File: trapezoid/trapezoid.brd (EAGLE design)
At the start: 59.7 x 28.6 mm, 32 parts, among them IC2 LGD20H, U1 MMA8452Q, U2 microSD, U4 MCP73831, Y1 CRYSTAL.ABS25

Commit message: small tweak
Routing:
- net GND: vias 9 -> 10
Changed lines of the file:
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@@
 <via x="14.605" y="19.685" extent="1-16" drill="0.508"/>
 <via x="20.32" y="5.08" extent="1-16" drill="0.508"/>
+<via x="57.15" y="16.51" extent="1-16" drill="0.508"/>
 </signal>
 <signal name="SCL">

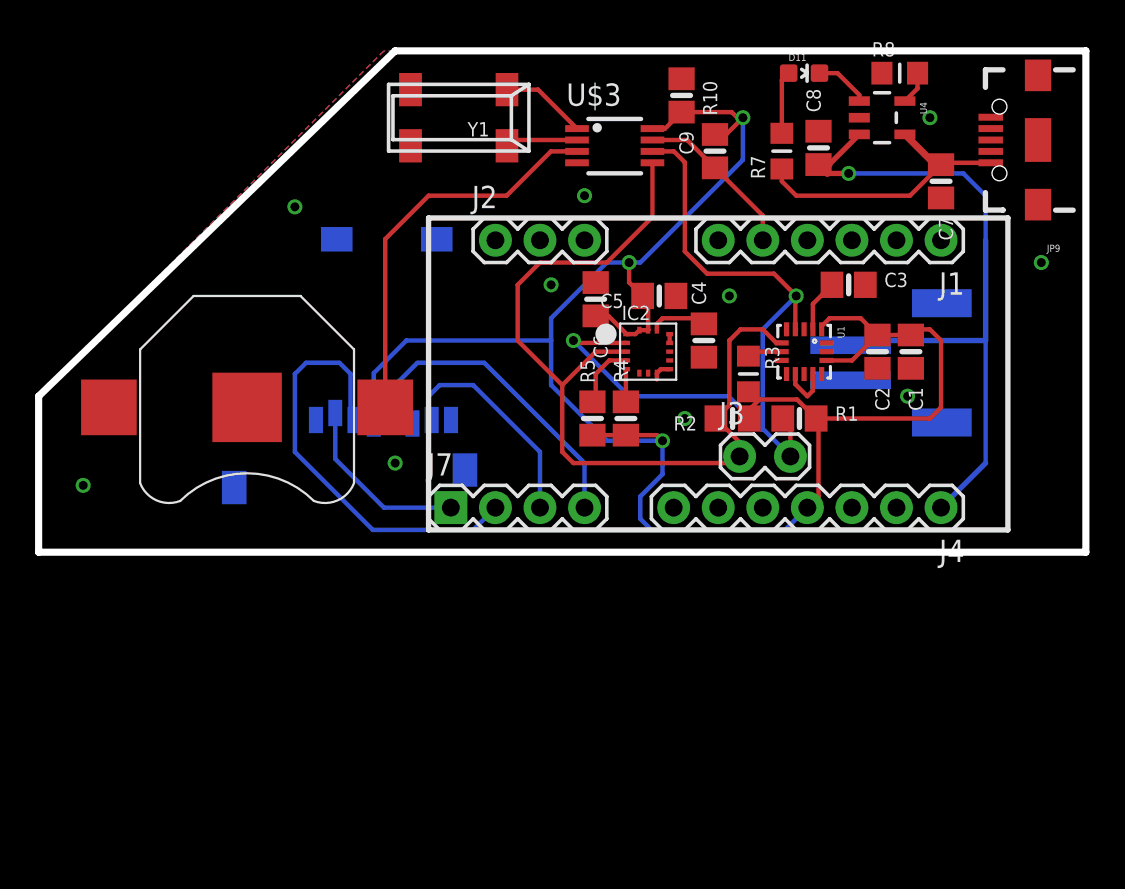
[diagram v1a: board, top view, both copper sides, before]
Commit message: changed gyro in schematic
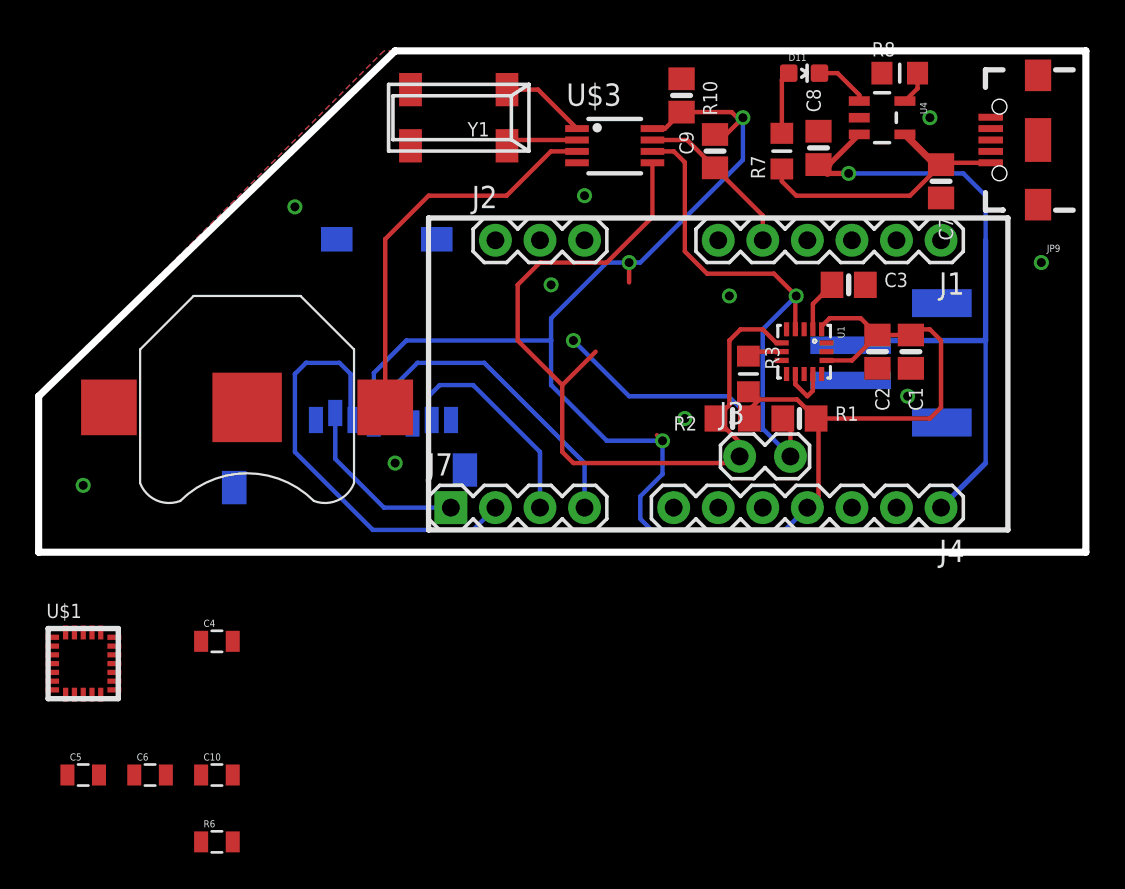
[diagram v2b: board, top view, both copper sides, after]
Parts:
- removed IC2: LGD20H, microbuilder:L3GD20H_LGA16L
- removed R4, R5: 10K, microbuilder:0805-NO
- added C10: 1.0uF, SparkFun-Passives:0805
- added R6: 47k, SparkFun-Passives:0805
- added U$1: FXAS21002, sharkdunio:24QFN
- C4, C6: device microbuilder:0805-NO -> SparkFun-Passives:0805
- C5: value 10uF -> 0.1uF; device microbuilder:0805-NO -> SparkFun-Passives:0805
- moved C5 42.7 mm to (2.54, -12.7), turned to 0 degrees
- moved C6 37.2 mm to (6.35, -12.7), turned to 0 degrees
- moved C4 32.6 mm to (10.2, -5.08), turned to 0 degrees
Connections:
- removed net CS_3.3V: IC2.5, R4.2
- removed net SDO/SAO: IC2.4, R5.2
- new net INT2: U$1.2
- new net N$9: R6.1, U$1.4
- net +3V3: now also C10.1, C4.2, C6.1, R6.2, U$1.15, U$1.17, U$1.18; no longer C5.2, C6.2, IC2.1, IC2.15, IC2.16, R4.1, R5.1
- net GND: now also C10.2, C5.2, C6.2, U$1.1, U$1.10, U$1.13, U$1.14, U$1.19, U$1.20, U$1.21, U$1.22, U$1.23, U$1.24, U$1.5, U$1.6, U$1.7, U$1.8, U$1.9; no longer C5.1, C6.1, IC2.10, IC2.11, IC2.12, IC2.13, IC2.8, IC2.9
- net N$3: now also C5.1, U$1.16; no longer C4.2, IC2.14
- net SCL: now also U$1.11; no longer IC2.2
- net SDA: now also U$1.12; no longer IC2.3
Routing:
- net +3V3: track 111.1 -> 100.7 mm
- net SDO/SAO: track 3.75 -> 0.00 mm
- net N$3: track 3.30 -> 0.00 mm
- net SCL: track 45.5 -> 42.6 mm
- net CS_3.3V: track 1.88 -> 0.00 mm
- net SDA: track 49.0 -> 47.2 mm
- net GND: track 4.90 -> 3.22 mm

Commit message: fully routed board
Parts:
- removed R6: 47k, SparkFun-Passives:0805
- added R4: 47K, microbuilder:0805-NO
- C10: value 1.0uF -> 0.1uF; device SparkFun-Passives:0805 -> microbuilder:0805-NO
- C4, C5, C6: device SparkFun-Passives:0805 -> microbuilder:0805-NO
- moved C5 38.2 mm to (31.1, 12.7), turned to 90 degrees
- moved U$1 38.1 mm to (35.6, 12.7), turned to 180 degrees
- moved C6 33.8 mm to (28.6, 12.7), turned to 90 degrees
- moved C10 32.3 mm to (33.7, 9.53), turned to 180 degrees
- moved C4 24.5 mm to (29.8, 9.53), turned to 180 degrees
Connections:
- removed net INT2: U$1.2
- net +3V3: now also C10.2, C5.2, C6.2, R4.2; no longer C10.1, C4.2, C6.1, R6.2
- net GND: now also C10.1, C4.2, C5.1, C6.1; no longer C10.2, C4.1, C5.2, C6.2
- net N$3: now also C4.1; no longer C5.1
- net N$9: now also R4.1; no longer R6.1
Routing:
- net +3V3: track 100.7 -> 120.4 mm
- net SCL: track 42.6 -> 33.6 mm, vias 2 -> 1
- net N$3: track 0.00 -> 5.55 mm
- net GND: track 3.22 -> 7.30 mm, vias 10 -> 11
- net N$9: track 0.00 -> 4.07 mm
- net SDA: track 47.2 -> 49.8 mm

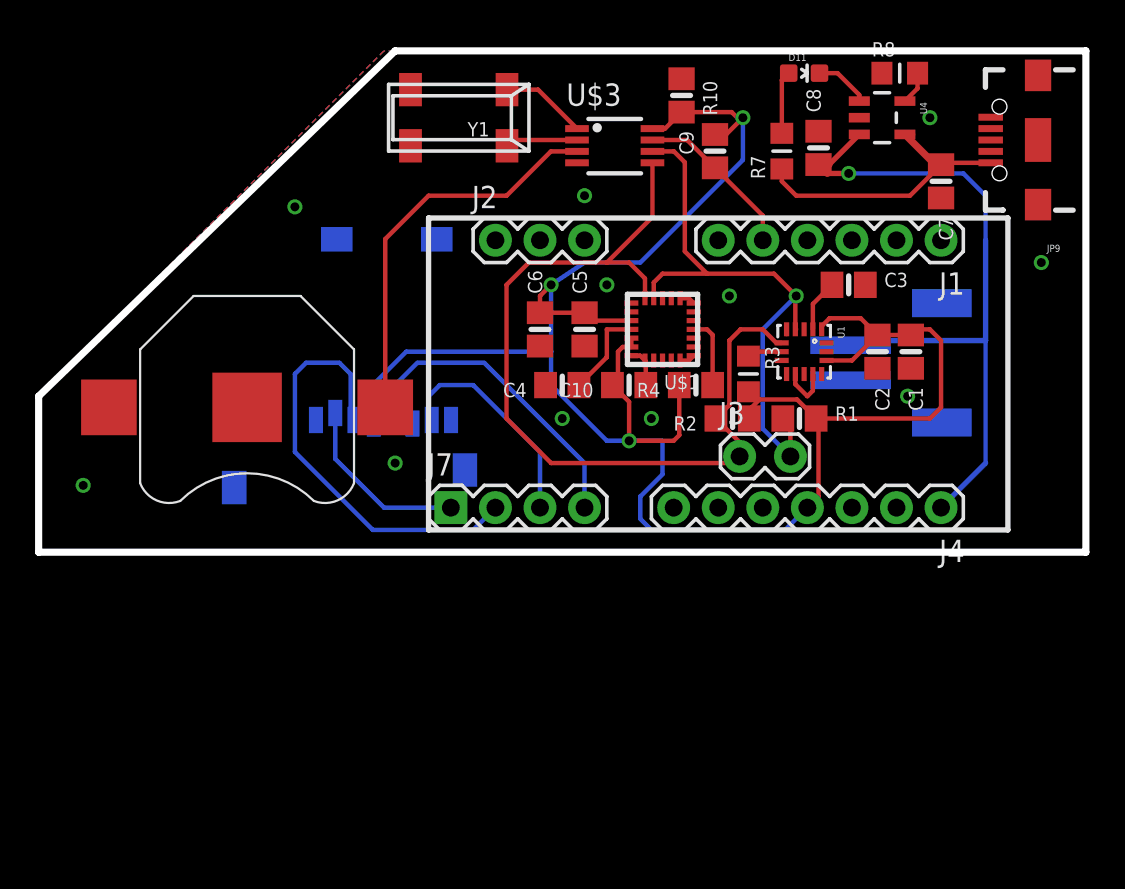
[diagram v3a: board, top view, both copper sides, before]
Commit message: shortend routes
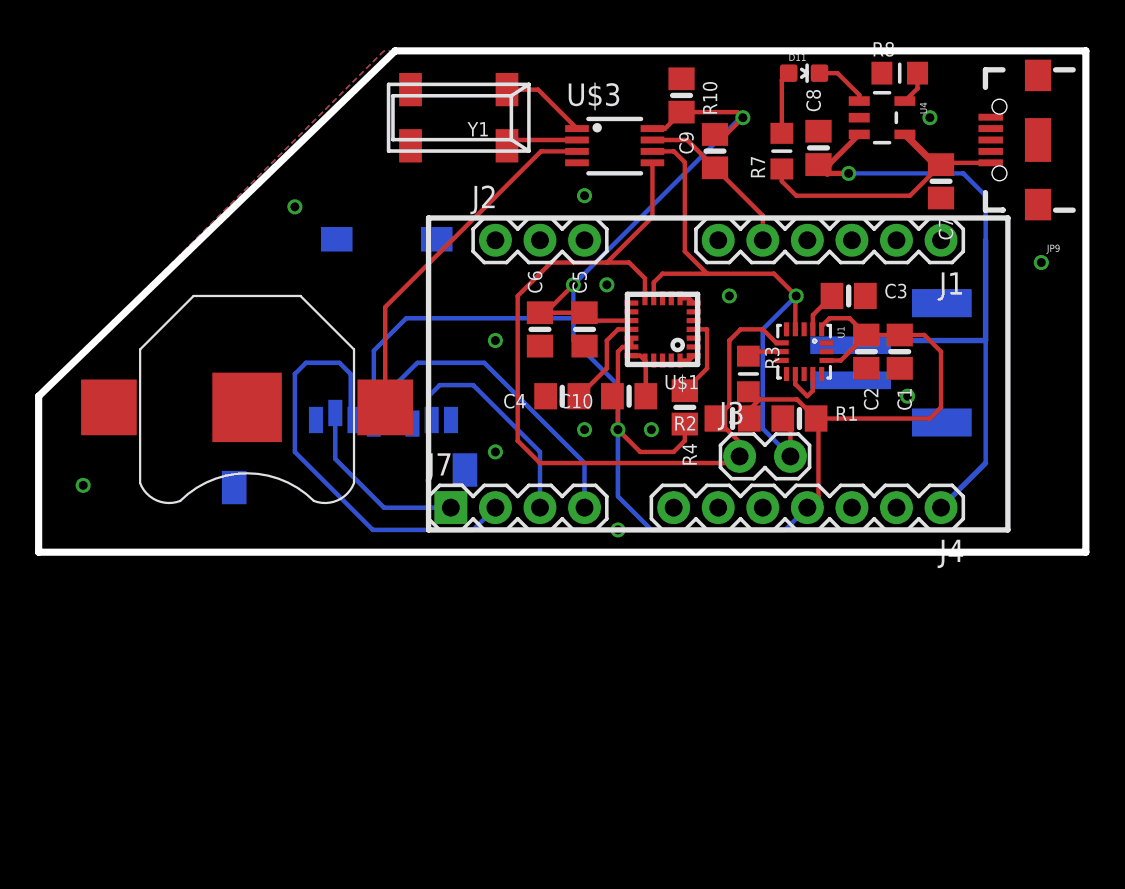
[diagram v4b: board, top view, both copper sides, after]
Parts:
- moved R4 1.42 mm to (36.8, 8.26), turned to 270 degrees
- moved C1 0.64 mm to (49.1, 11.4)
- moved C2 0.64 mm to (47.2, 11.4)
- moved C10 0.63 mm to (33.7, 8.89)
- moved C3 0.63 mm to (46.2, 14.6)
- moved C4 0.63 mm to (29.8, 8.89)
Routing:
- net +3V3: track 120.4 -> 115.4 mm
- net N$4: track 22.6 -> 20.3 mm
- net N$9: track 4.07 -> 5.24 mm
- net SDA: track 49.8 -> 48.9 mm
- net GND: track 7.30 -> 7.94 mm, vias 11 -> 13
- net BYP: track 2.99 -> 2.35 mm

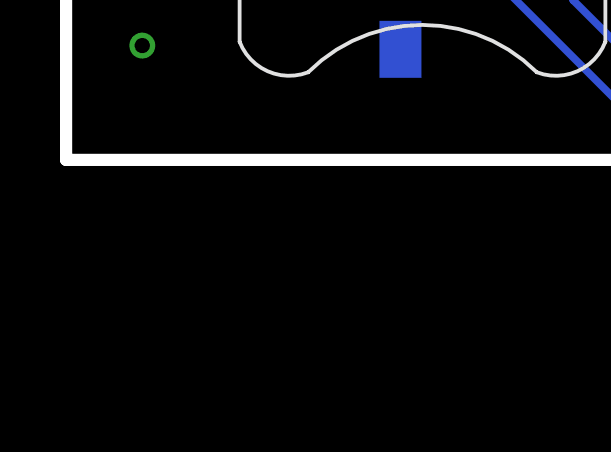
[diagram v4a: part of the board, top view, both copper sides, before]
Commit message: add raw voltage headers
allow for easy attachment of inductive charging
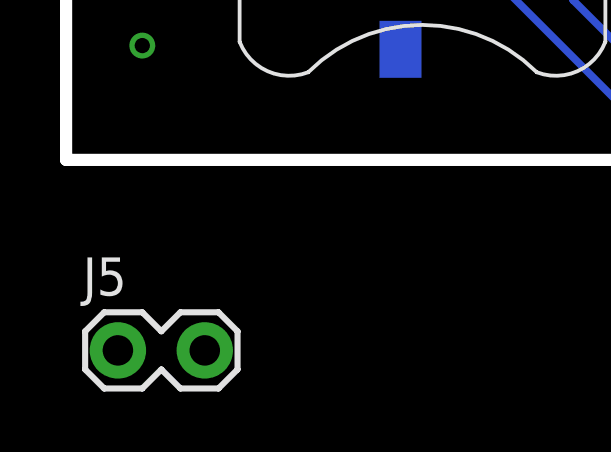
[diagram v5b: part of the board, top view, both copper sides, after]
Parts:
- added J5: (no value), SparkFun-Connectors:1X02_LOCK
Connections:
- net GND: now also J5.1
- net V_RAW: now also J5.2
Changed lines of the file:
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@@
 <grid distance="0.025" unitdist="inch" unit="inch" style="lines" multiple="1" display="yes" altdistance="0.025" altunitdist="inch" altunit="inch"/>
 <layers>
-<layer number="1" name="Top" color="4" fill="1" visible="no" active="yes"/>
+<layer number="1" name="Top" color="4" fill="1" visible="yes" active="yes"/>
 <layer number="2" name="Route2" color="1" fill="3" visible="no" active="no"/>
 <layer number="3" name="Route3" color="4" fill="3" visible="no" active="no"/>
@@
 <element name="C5" library="microbuilder" package="0805-NO" value="0.1uF" x="31.115" y="12.7" rot="R90"/>
 <element name="C6" library="microbuilder" package="0805-NO" value="0.1uF" x="28.575" y="12.7" rot="R90"/>
+<element name="J5" library="SparkFun-Connectors" package="1X02_LOCK" value="" x="1.905" y="-6.35"/>
 </elements>
 <signals>
@@
 <via x="33.02" y="1.27" extent="1-16" drill="0.508"/>
 <via x="26.035" y="12.065" extent="1-16" drill="0.508"/>
+<contactref element="J5" pad="1"/>
+<wire x1="2.54" y1="3.81" x2="1.7272" y2="-6.35" width="0" layer="19" extent="1-1"/>
 </signal>
 <signal name="SCL">
@@
 <wire x1="53.975" y1="17.78" x2="53.975" y2="20.32" width="0.254" layer="16"/>
 <wire x1="53.975" y1="20.32" x2="52.705" y2="21.59" width="0.254" layer="16"/>
+<contactref element="J5" pad="2"/>
+<wire x1="4.6228" y1="-6.35" x2="46.28" y2="11.795" width="0" layer="19" extent="16-16"/>
 </signal>
 <signal name="+3V3">
